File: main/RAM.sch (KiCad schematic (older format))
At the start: 5 parts, among them U63 74LS08, U64 628128_DIP32_SSOP32, U65 74LS245, U66 74LS04, U67 28C256

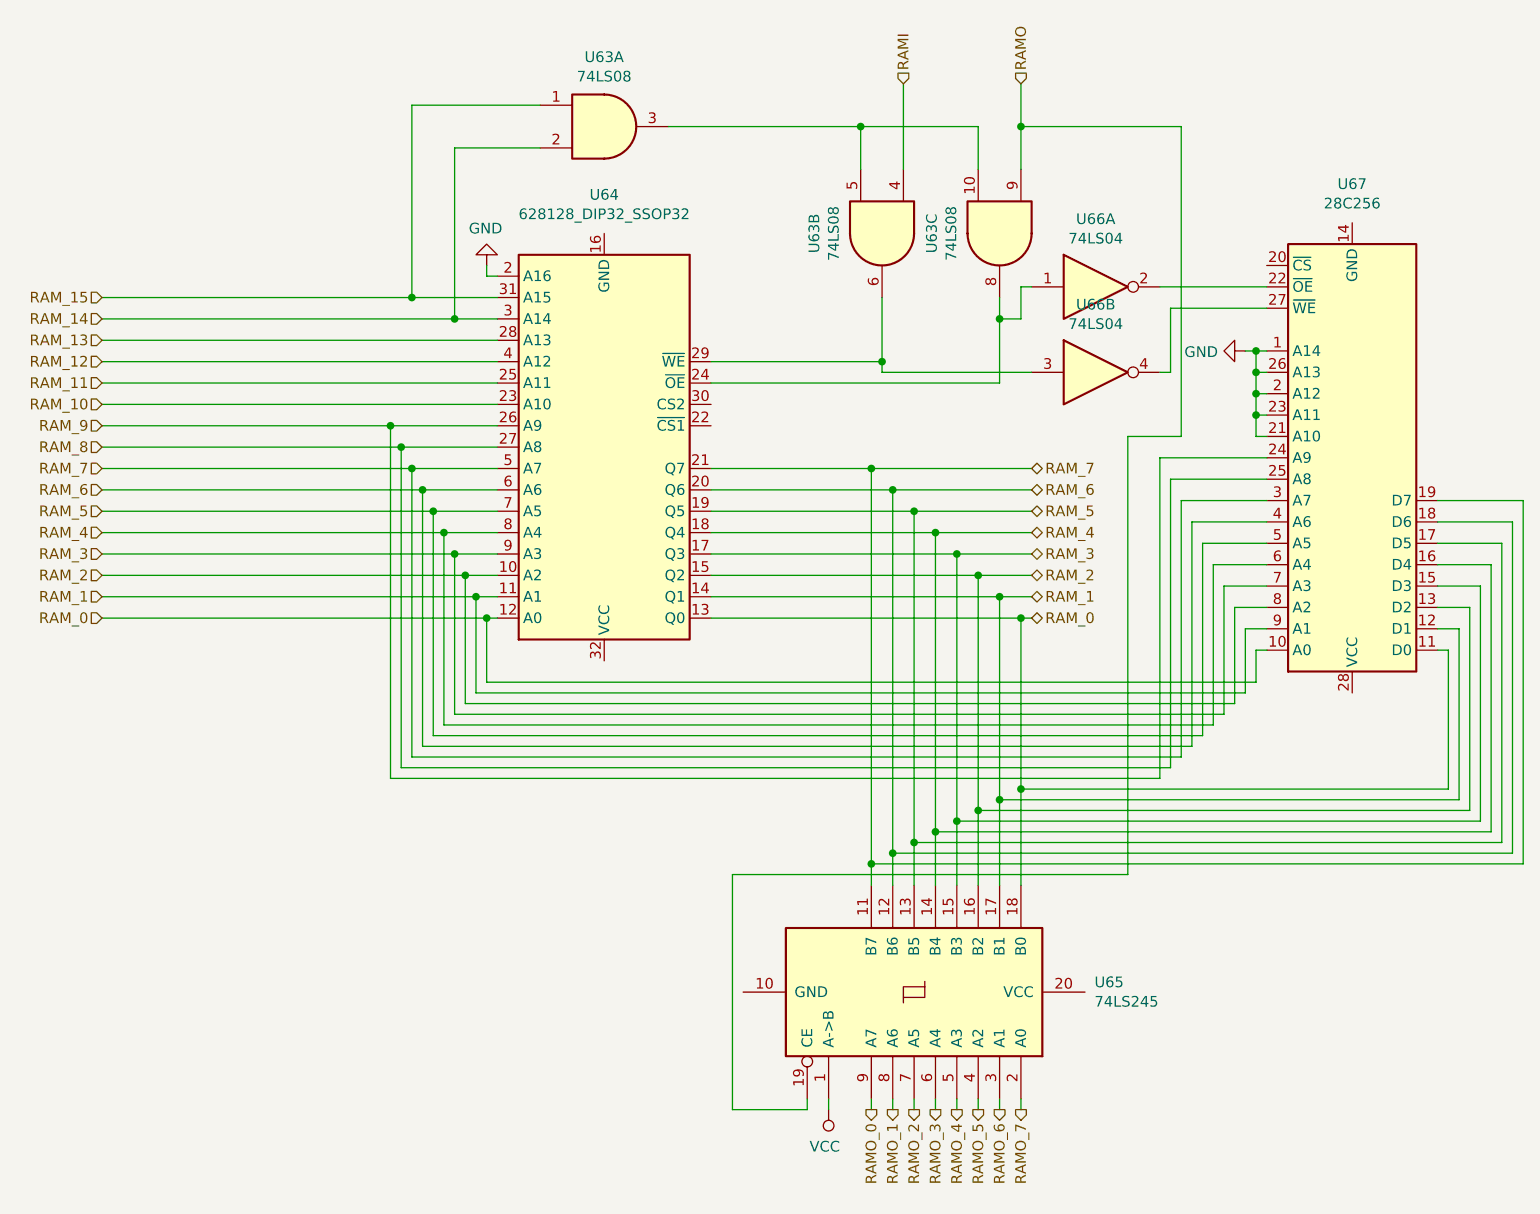
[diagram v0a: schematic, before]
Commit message: Replot main with symbols
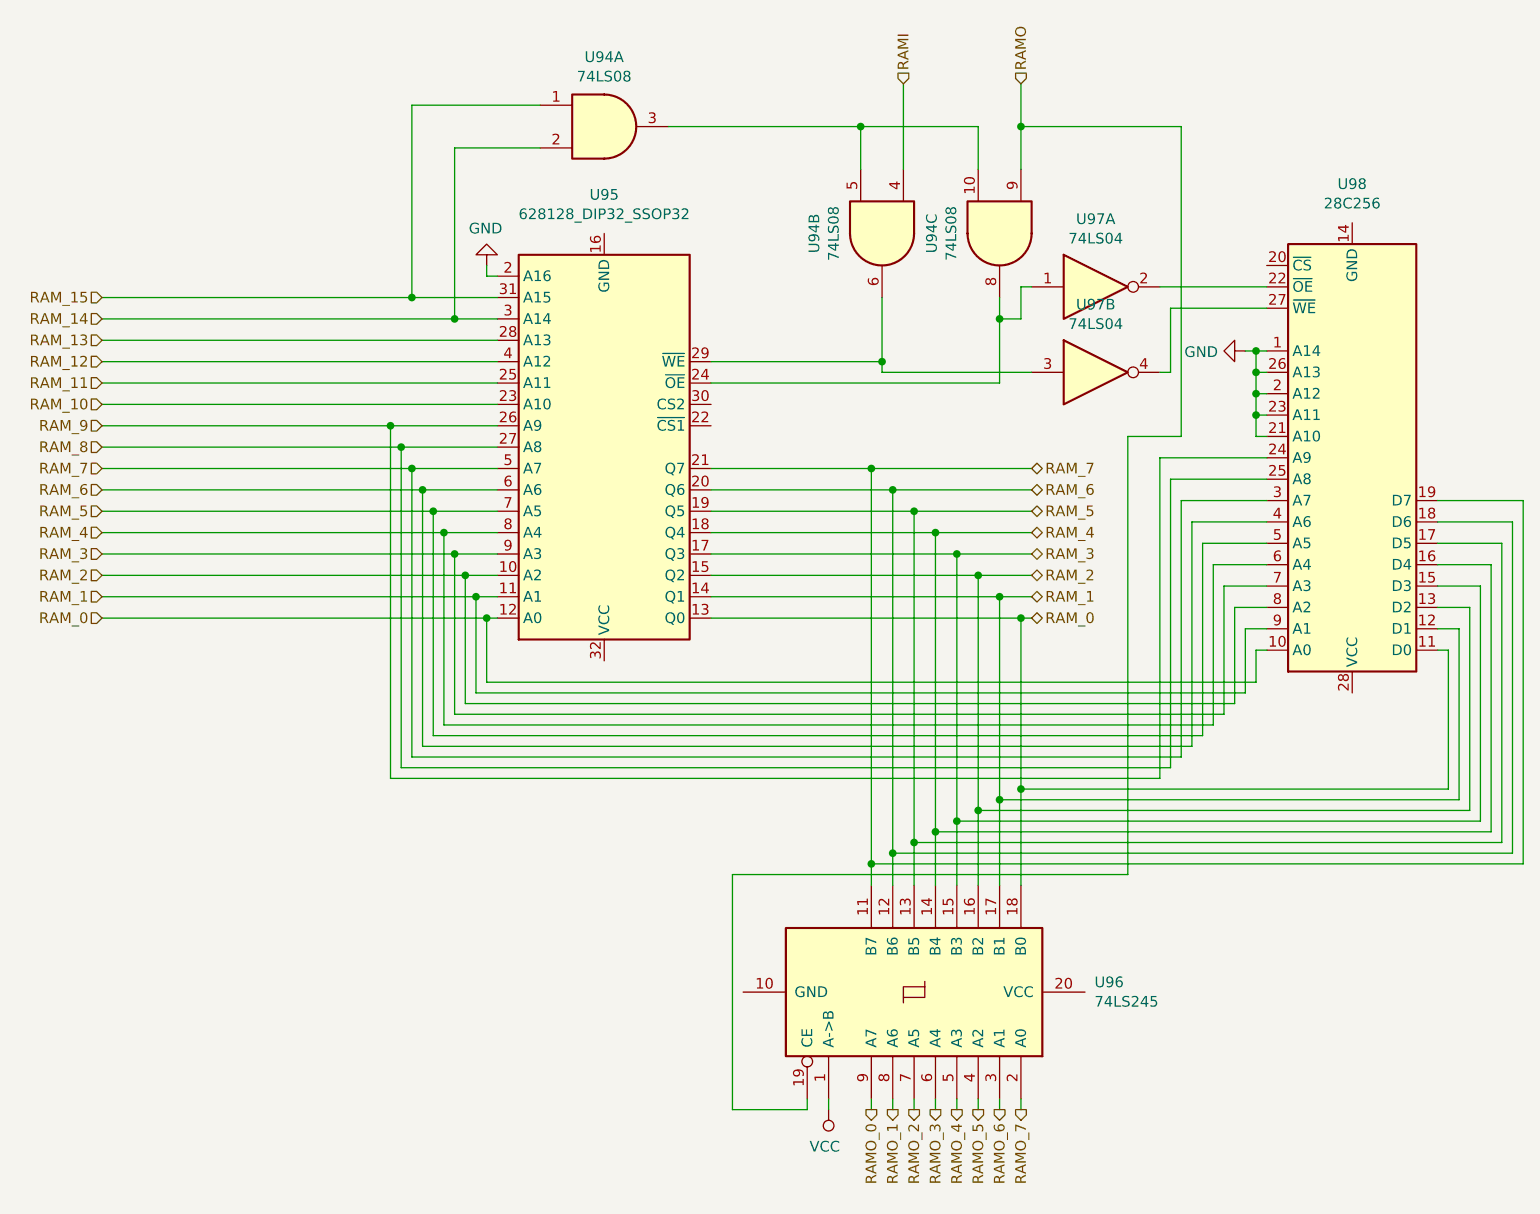
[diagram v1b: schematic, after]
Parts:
- renumbered U63 to U94, U64 to U95, U65 to U96, U66 to U97, U67 to U98
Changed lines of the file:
@@
 Sheet 25 26
 Title "Memory"
-Date "2019-11-13"
+Date "2019-11-17"
 Rev "v1.0"
 Comp "Christopher Milan"
@@
 P 4500 2950
 AR Path="/5E5B2276/5D858701" Ref="U?"  Part="1"
-AR Path="/5E5B2276/5D857448/5D858701" Ref="U64"  Part="1"
-F 0 "U64" H 4500 1769 50  0000 C CNN
+AR Path="/5E5B2276/5D857448/5D858701" Ref="U95"  Part="1"
+F 0 "U95" H 4500 1769 50  0000 C CNN
 F 1 "628128_DIP32_SSOP32" H 4500 1860 50  0000 C CNN
 F 2 "" H 4500 2950 50  0001 C CNN
@@
 RAM_15
 $Comp
-L 74xx:74LS08 U63
+L 74xx:74LS08 U94
 U 2 1 5D86123E
 P 5800 1950
-F 0 "U63" H 5800 1633 50  0000 C CNN
+F 0 "U94" H 5800 1633 50  0000 C CNN
 F 1 "74LS08" H 5800 1724 50  0000 C CNN
 F 2 "" H 5800 1950 50  0001 C CNN
@@
 $EndComp
 $Comp
-L 74xx:74LS08 U63
+L 74xx:74LS08 U94
 U 3 1 5D86652B
 P 6350 1950
-F 0 "U63" H 6350 1633 50  0000 C CNN
+F 0 "U94" H 6350 1633 50  0000 C CNN
 F 1 "74LS08" H 6350 1724 50  0000 C CNN
 F 2 "" H 6350 1950 50  0001 C CNN
@@
 	6450 1250 6450 1450
 $Comp
-L Memory_EEPROM:28C256 U67
+L Memory_EEPROM:28C256 U98
 U 1 1 5D886118
 P 8000 3000
-F 0 "U67" H 8000 1719 50  0000 C CNN
+F 0 "U98" H 8000 1719 50  0000 C CNN
 F 1 "28C256" H 8000 1810 50  0000 C CNN
 F 2 "" H 8000 3000 50  0001 C CNN
@@
 	5000 2650 6350 2650
 $Comp
-L 74xx:74LS04 U66
+L 74xx:74LS04 U97
 U 1 1 5D8C76E3
 P 6800 2200
-F 0 "U66" H 6800 2517 50  0000 C CNN
+F 0 "U97" H 6800 2517 50  0000 C CNN
 F 1 "74LS04" H 6800 2426 50  0000 C CNN
 F 2 "" H 6800 2200 50  0001 C CNN
@@
 $EndComp
 $Comp
-L 74xx:74LS04 U66
+L 74xx:74LS04 U97
 U 2 1 5D8CAB5C
 P 6800 2600
-F 0 "U66" H 6800 2917 50  0000 C CNN
+F 0 "U97" H 6800 2917 50  0000 C CNN
 F 1 "74LS04" H 6800 2826 50  0000 C CNN
 F 2 "" H 6800 2600 50  0001 C CNN
@@
 	7550 4050 7550 3900
 $Comp
-L 74xx:74LS08 U63
+L 74xx:74LS08 U94
 U 1 1 5DB08B15
 P 4500 1450
-F 0 "U63" H 4500 1775 50  0000 C CNN
+F 0 "U94" H 4500 1775 50  0000 C CNN
 F 1 "74LS08" H 4500 1684 50  0000 C CNN
 F 2 "" H 4500 1450 50  0001 C CNN
@@
 $EndComp
 $Comp
-L 74xx:74LS245 U65
+L 74xx:74LS245 U96
 U 1 1 5DB0B306
 P 5950 5500
-F 0 "U65" V 5996 6344 50  0000 L CNN
+F 0 "U96" V 5996 6344 50  0000 L CNN
 F 1 "74LS245" V 5905 6344 50  0000 L CNN
 F 2 "" H 5950 5500 50  0001 C CNN
